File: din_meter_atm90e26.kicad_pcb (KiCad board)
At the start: 2 copper layers, 29 x 31.2 mm, 60 parts, among them J1 USEL, J2 MMD1, J3 MMD0, J4 CONN_02X18, J5 CONN_01X10, J6 USEL, J7 MMD1, J8 MMD0, M1 ATM90E26_ATM90E26, M2 ATM90E26_ATM90E26, Y1 Crystal_Small, Y2 Crystal_Small

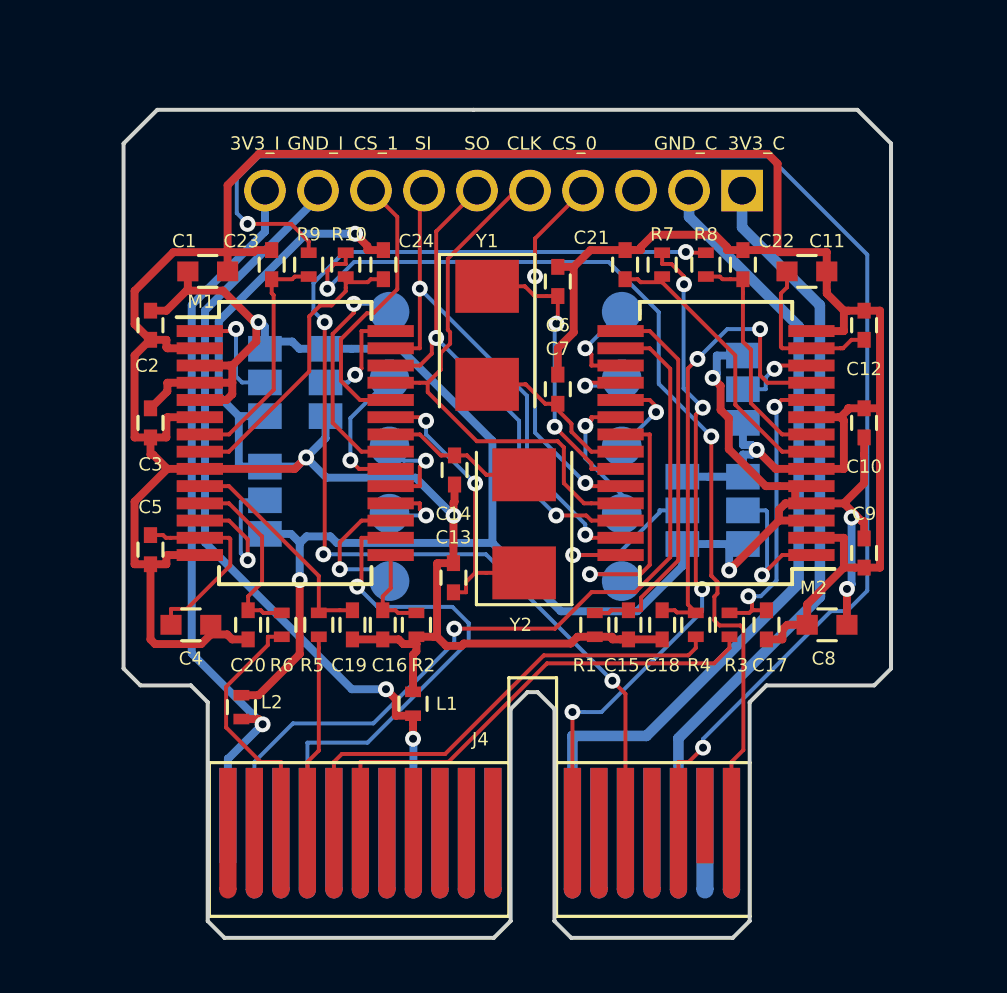
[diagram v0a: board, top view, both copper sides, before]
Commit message: Moved some tracks up to reduce exposure
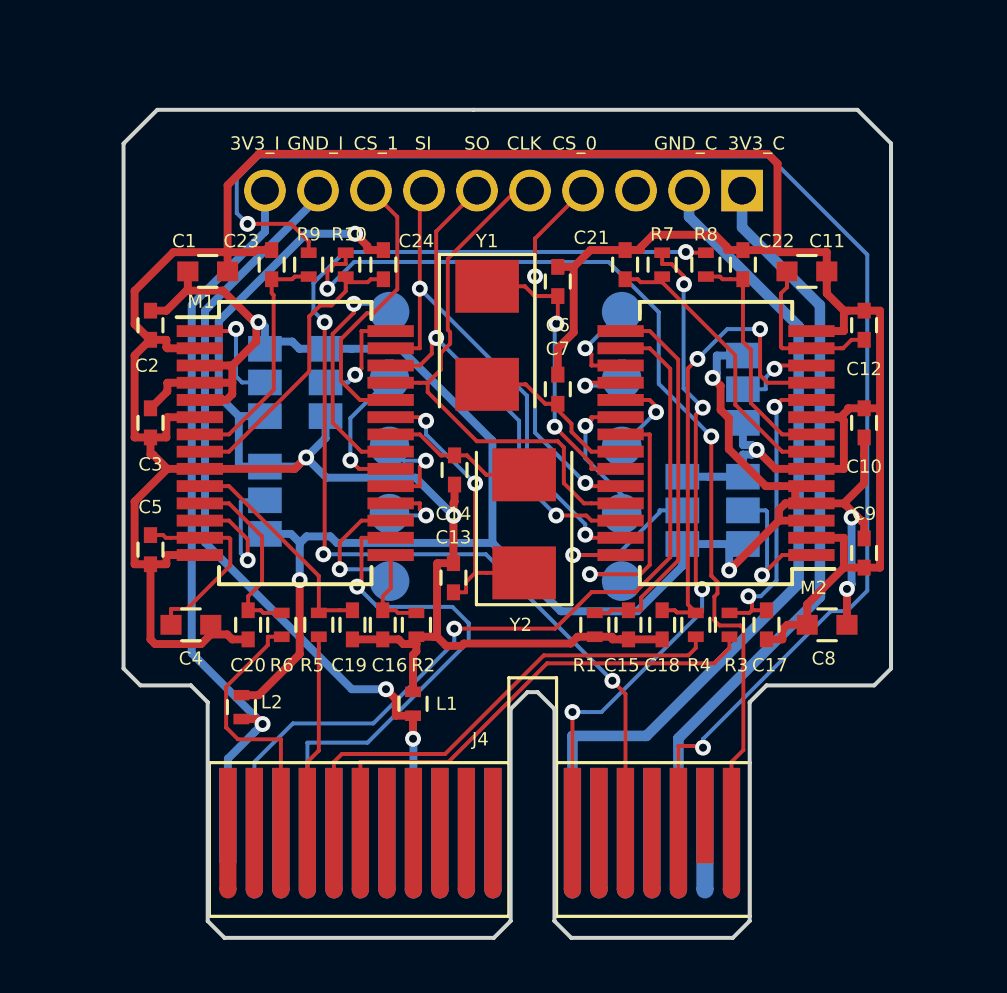
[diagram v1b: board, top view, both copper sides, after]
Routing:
- net I1N_1_IN: track 9.73 -> 10.2 mm
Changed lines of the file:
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@@
   (segment (start 141.649 75.091) (end 141.649 76.3507) (width 0.15) (layer F.Cu) (net 37))
   (segment (start 141.351 77.174) (end 141.351 76.6487) (width 0.15) (layer F.Cu) (net 37))
-  (via (at 136.8179 81.4779) (size 0.6) (layers F.Cu B.Cu) (net 38))
-  (segment (start 136.017 81.28) (end 136.6673 81.28) (width 0.3) (layer F.Cu) (net 38))
-  (segment (start 135.5231 82.7727) (end 136.8179 81.4779) (width 0.3) (layer B.Cu) (net 38))
-  (segment (start 135.508 82.7727) (end 135.5231 82.7727) (width 0.3) (layer B.Cu) (net 38))
-  (segment (start 136.6673 81.3273) (end 136.6673 81.28) (width 0.3) (layer F.Cu) (net 38))
-  (segment (start 136.8179 81.4779) (end 136.6673 81.3273) (width 0.3) (layer F.Cu) (net 38))
-  (segment (start 135.508 84.923) (end 135.508 82.7727) (width 0.3) (layer B.Cu) (net 38))
-  (segment (start 134.1446 78.8046) (end 136.8179 81.4779) (width 0.3) (layer B.Cu) (net 38))
-  (segment (start 134.1446 65.6554) (end 134.1446 78.8046) (width 0.3) (layer B.Cu) (net 38))
+  (segment (start 134.1446 78.79369) (end 136.517901 81.166991) (width 0.3) (layer B.Cu) (net 38))
+  (via (at 136.8179 81.46699) (size 0.6) (drill 0.3) (layers F.Cu B.Cu) (net 38))
+  (segment (start 134.1446 65.6554) (end 134.1446 78.79369) (width 0.3) (layer B.Cu) (net 38))
   (segment (start 136.907 62.893) (end 134.1446 65.6554) (width 0.3) (layer B.Cu) (net 38))
+  (segment (start 136.017 81.28) (end 136.63091 81.28) (width 0.3) (layer F.Cu) (net 38))
+  (segment (start 136.517901 81.766989) (end 136.8179 81.46699) (width 0.3) (layer B.Cu) (net 38))
   (segment (start 136.907 61.341) (end 136.907 62.893) (width 0.3) (layer B.Cu) (net 38))
+  (segment (start 135.508 84.923) (end 135.508 82.77689) (width 0.3) (layer B.Cu) (net 38))
+  (segment (start 136.63091 81.28) (end 136.8179 81.46699) (width 0.3) (layer F.Cu) (net 38))
+  (segment (start 135.508 82.77689) (end 136.517901 81.766989) (width 0.3) (layer B.Cu) (net 38))
+  (segment (start 136.517901 81.166991) (end 136.8179 81.46699) (width 0.3) (layer B.Cu) (net 38))
+  (segment (start 137.0157 78.174) (end 137.541 78.174) (width 0.15) (layer F.Cu) (net 39))
+  (segment (start 135.4412 81.5954) (end 135.4412 80.0626) (width 0.15) (layer F.Cu) (net 39))
+  (segment (start 137.508 85.423) (end 137.508 82.042) (width 0.15) (layer F.Cu) (net 39))
+  (segment (start 137.508 82.042) (end 135.8878 82.042) (width 0.15) (layer F.Cu) (net 39))
+  (segment (start 135.4412 80.0626) (end 137.0157 78.4881) (width 0.15) (layer F.Cu) (net 39))
+  (segment (start 135.8878 82.042) (end 135.4412 81.5954) (width 0.15) (layer F.Cu) (net 39))
   (segment (start 137.0157 78.4881) (end 137.0157 78.174) (width 0.15) (layer F.Cu) (net 39))
-  (segment (start 135.4412 80.0626) (end 137.0157 78.4881) (width 0.15) (layer F.Cu) (net 39))
-  (segment (start 135.4412 81.5954) (end 135.4412 80.0626) (width 0.15) (layer F.Cu) (net 39))
-  (segment (start 136.7435 82.8977) (end 135.4412 81.5954) (width 0.15) (layer F.Cu) (net 39))
-  (segment (start 137.508 82.8977) (end 136.7435 82.8977) (width 0.15) (layer F.Cu) (net 39))
-  (segment (start 137.508 85.423) (end 137.508 82.8977) (width 0.15) (layer F.Cu) (net 39))
-  (segment (start 137.541 78.174) (end 137.0157 78.174) (width 0.15) (layer F.Cu) (net 39))
   (segment (start 134.449 72.491) (end 135.5493 72.491) (width 0.15) (layer F.Cu) (net 40))
   (segment (start 140.208 77.174) (end 139.7327 77.174) (width 0.15) (layer F.Cu) (net 40))
@@
   (segment (start 153.162 69.7929) (end 153.162 76.1403) (width 0.15) (layer F.Cu) (net 48))
   (segment (start 153.4232 69.5317) (end 153.162 69.7929) (width 0.15) (layer F.Cu) (net 48))
+  (segment (start 152.508 85.423) (end 152.508 82.296) (width 0.15) (layer F.Cu) (net 49))
+  (segment (start 152.508 82.296) (end 153.3731 82.296) (width 0.15) (layer F.Cu) (net 49))
+  (segment (start 153.3731 82.296) (end 153.4353 82.3582) (width 0.15) (layer F.Cu) (net 49))
   (via (at 153.4353 82.3582) (size 0.6) (layers F.Cu B.Cu) (net 49))
   (via (at 136.2509 62.5968) (size 0.6) (layers F.Cu B.Cu) (net 49))
@@
   (segment (start 137.8941 62.5968) (end 138.557 63.2597) (width 0.15) (layer F.Cu) (net 49))
   (segment (start 136.2509 62.5968) (end 137.8941 62.5968) (width 0.15) (layer F.Cu) (net 49))
-  (segment (start 152.508 85.423) (end 152.508 82.8977) (width 0.15) (layer F.Cu) (net 49))
   (segment (start 153.4353 82.03) (end 153.4353 82.3582) (width 0.15) (layer B.Cu) (net 49))
   (segment (start 158.2566 77.2087) (end 153.4353 82.03) (width 0.15) (layer B.Cu) (net 49))
@@
   (segment (start 135.8441 62.19) (end 135.8441 60.8963) (width 0.15) (layer B.Cu) (net 49))
   (segment (start 136.2509 62.5968) (end 135.8441 62.19) (width 0.15) (layer B.Cu) (net 49))
-  (segment (start 152.8958 82.8977) (end 153.4353 82.3582) (width 0.15) (layer F.Cu) (net 49))
-  (segment (start 152.508 82.8977) (end 152.8958 82.8977) (width 0.15) (layer F.Cu) (net 49))
   (via (at 150.0144 79.8343) (size 0.6) (layers F.Cu B.Cu) (net 50))
   (via (at 139.1113 75.0634) (size 0.6) (layers F.Cu B.Cu) (net 50))

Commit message: Rerouted board from joslyn
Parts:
- removed G1: LOGO, Whatnick_logo:Whatnick_logo
- removed LOGO1: Logo_Open_Hardware_Small, Symbols:OSHW-Logo2_7.3x6mm_SilkScreen
- moved L2 21.1 mm to (132.8, 60.0), turned to 0 degrees
- moved L1 20.9 mm to (132.8, 62.1), turned to 0 degrees
- moved C23 15.0 mm to (143.2, 77.9), turned to 90 degrees
- moved R9 15.0 mm to (144.4, 77.9), turned to 270 degrees
- moved C15 14.5 mm to (153.2, 63.4), turned to 180 degrees
- moved R1 14.4 mm to (150.9, 63.4), turned to 180 degrees
- moved R10 13.9 mm to (141.9, 77.9), turned to 270 degrees
- moved C22 13.9 mm to (153.2, 77.9), turned to 90 degrees
- moved R8 13.8 mm to (154.4, 77.9), turned to 270 degrees
- moved C24 13.8 mm to (140.7, 77.9), turned to 90 degrees
- moved C21 13.7 mm to (156.2, 76.6), turned to 90 degrees
- moved R7 13.6 mm to (157.4, 76.6), turned to 270 degrees
- moved ZX_0 6.12 mm to (152.7, 70.4)
- moved C8 5.18 mm to (159.2, 72.7), turned to 270 degrees
- moved C17 5.17 mm to (150.7, 77.9)
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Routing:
- net GNDD: track 165.3 -> 108.0 mm, vias 4 -> 37
- net I2P_1_IN: track 56.2 -> 16.9 mm
- net I2N_0_IN: track 44.4 -> 10.3 mm, vias 4 -> 0
- net I2N_1_IN: track 37.2 -> 20.4 mm
- net GND_ISO: track 30.2 -> 44.6 mm, vias 2 -> 1
- net GND_CPU: track 31.0 -> 45.2 mm, vias 0 -> 2
- net SI/RX: track 20.4 -> 34.2 mm, vias 2 -> 3
- net 3V3_CPU: track 27.5 -> 38.3 mm
- net VN_0: track 14.4 -> 4.88 mm
- net I2P_0_IN: track 25.5 -> 16.0 mm, vias 4 -> 2
- net 3V3_ISO: track 27.3 -> 36.5 mm
- net I2N_0: track 9.01 -> 16.7 mm
- net I2P_0: track 11.0 -> 18.3 mm
- net I2P_1: track 9.12 -> 15.9 mm
- net VP_0: track 31.0 -> 37.8 mm, vias 1 -> 3
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- added copper zone on B.Cu, net GNDD
- added copper zone on F.Cu, net GNDD
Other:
- board size 29 x 31.2 mm -> 32 x 31.1 mm
- rule pad_to_mask_clearance: 0.2 -> 0.15

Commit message: Add back logos and bump version
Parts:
- added G1: LOGO, Whatnick_logo:Whatnick_logo, B.Cu at (140.4, 78.3)
- added LOGO1: Logo_Open_Hardware_Small, Symbols:OSHW-Logo2_7.3x6mm_SilkScreen, B.Cu at (133.3, 69.7)
- added SYM1: SYM_Flash_Small, Whatnick_logo:Fsilk_HV, B.Cu at (158.5, 70.3)
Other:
- net class Default: trace_width 0.15 -> 0.25
- board text added: "Dual ATM90E26 Metering v1.1 22/11/2017"
- board text removed: "Dual ATM90E26 v0.1 16/10/2017"
